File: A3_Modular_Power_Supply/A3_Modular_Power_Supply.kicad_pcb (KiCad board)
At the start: 2 copper layers, 70.9 x 86.6 mm, 81 parts, among them J1 JST-XH, J10 JST-XH, J11 JST-XH, J12 JST-XH, J13 JST-XH, J14 JST-XH, J15 JST-XH, J16 JST-XH, J17 FX30B-3S-7.62DSA, J18 FX30B-3S-7.62DSA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

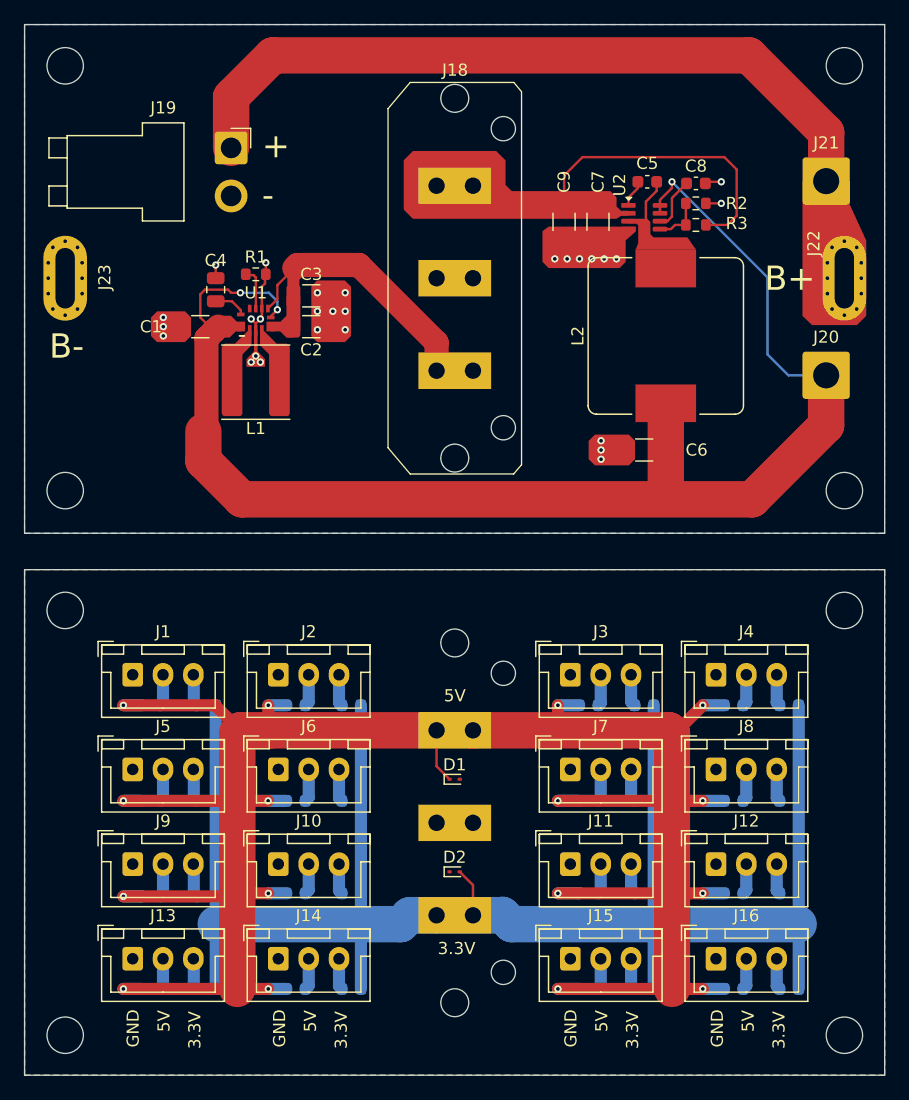
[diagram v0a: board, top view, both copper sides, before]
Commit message: Resized board to match flight computer Switched to single PCB
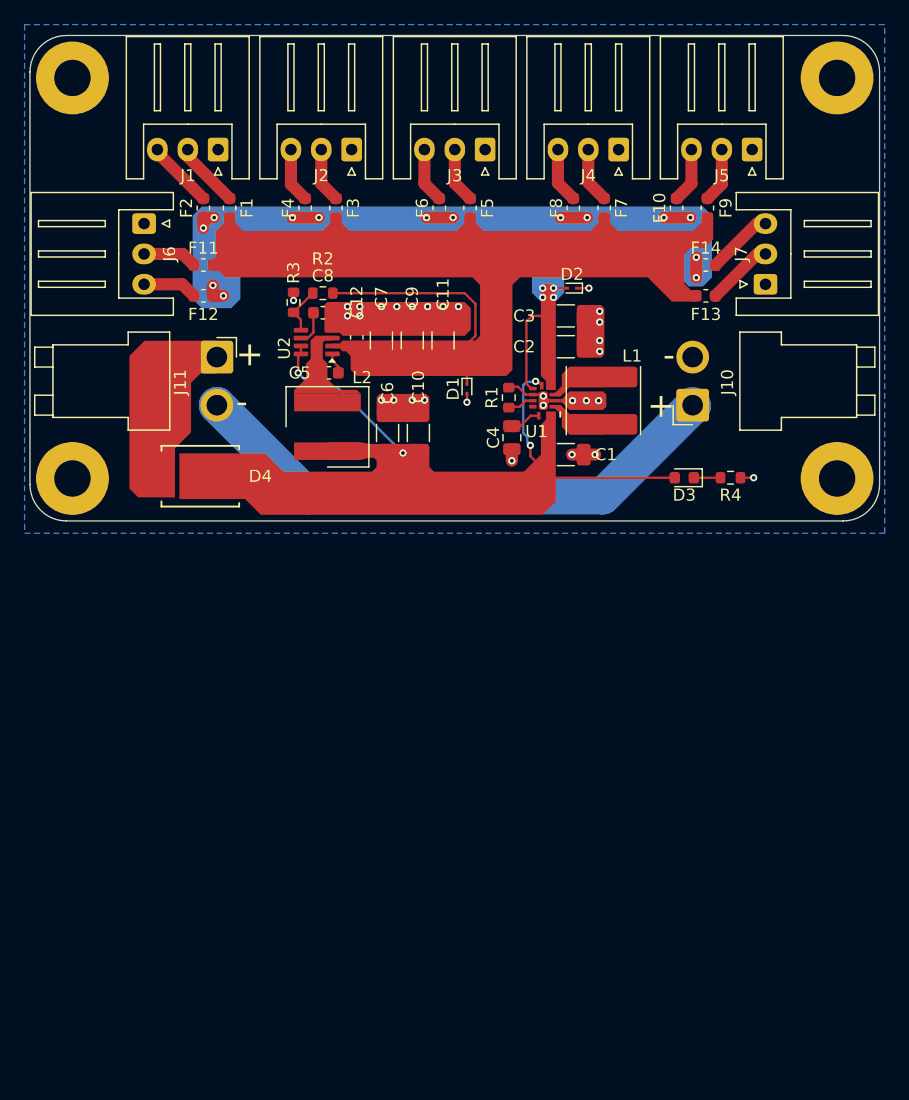
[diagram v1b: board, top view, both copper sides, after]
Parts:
- removed F15, F16, F17, F18, F19, F20, F21, F22, F23, F24, F25, F26, F27, F28, F29, F30, F31, F32: 1A, Fuse:Fuse_0603_1608Metric
- removed the J11 at (159.5, 123.3)
- removed J12, J13, J14, J15, J16, J8, J9: JST-XH, Connector_JST:JST_XH_B3B-XH-A_1x03_P2.50mm_Vertical
- removed J17, J18: FX30B-3S-7.62DSA, MPS_footprints:FX30B-3x-7.62
- removed J20: SWITCH-, Connector_Wire:SolderWire-1.5sqmm_1x01_D1.7mm_OD3.9mm
- removed J21: SWITCH+, Connector_Wire:SolderWire-1.5sqmm_1x01_D1.7mm_OD3.9mm
- removed J22: BATT+, MPS_footprints:Nickle_Strip
- removed J23: BATT-, MPS_footprints:Nickle_Strip
- removed the REF** at (182.1, 137.4)
- removed the REF** at (117.9, 102.4)
- removed the REF** at (182.1, 102.4)
- removed the REF** at (117.9, 137.4)
- removed the REF** at (117.9, 57.5)
- removed the REF** at (182.1, 57.5)
- removed the REF** at (117.9, 92.5)
- removed the REF** at (182.1, 92.5)
- added C10: 10uF, Capacitor_SMD:C_1206_3216Metric, F.Cu at (147.0, 87.8)
- added C11: 10uF, Capacitor_SMD:C_1206_3216Metric, F.Cu at (149.0, 80.1)
- added C12: 0.1uF, Capacitor_SMD:C_0603_1608Metric, F.Cu at (141.9, 79.9)
- added D3: LED, LED_SMD:LED_0603_1608Metric, F.Cu at (168.9, 91.4)
- added D4: STPS1045SFY, MPS_footprints:PSMCTO-277A_STM, F.Cu at (129.0, 91.3)
- added R4: 120R, Resistor_SMD:R_0603_1608Metric, F.Cu at (172.7, 91.4)
- added REF**: MountingHole_3mm_Pad, MountingHole:MountingHole_3mm_Pad, F.Cu at (181.5, 91.5)
- added REF**: MountingHole_3mm_Pad, MountingHole:MountingHole_3mm_Pad, F.Cu at (118.5, 91.5)
- added REF**: MountingHole_3mm_Pad, MountingHole:MountingHole_3mm_Pad, F.Cu at (181.5, 58.5)
- added REF**: MountingHole_3mm_Pad, MountingHole:MountingHole_3mm_Pad, F.Cu at (118.5, 58.5)
- F1, F10, F11, F12, F13, F14, F2, F3, F4, F5, F6, F7, F8, F9: moved to F.Cu
- J1, J2, J3, J4, J5, J6, J7: footprint Connector_JST:JST_XH_B3B-XH-A_1x03_P2.50mm_Vertical -> Connector_JST:JST_XH_S3B-XH-A_1x03_P2.50mm_Horizontal
- J10: value JST-XH -> BATT; footprint Connector_JST:JST_XH_B3B-XH-A_1x03_P2.50mm_Vertical -> Connector_JST:JST_VH_B2PS-VH_1x02_P3.96mm_Horizontal
- J11: renamed from J19; value Charge -> SWITCH
- L2: footprint Inductor_SMD:L_Bourns_SRP1245A -> MPS_footprints:L_Wurth_WE-XHMI-6060P
- moved J5 72.2 mm to (174.5, 64.4), turned to 180 degrees
- moved F9 67.0 mm to (170.8, 69.2), turned to -90 degrees
- moved F10 62.4 mm to (168.3, 69.2), turned to -90 degrees
- moved J10 50.9 mm to (169.6, 85.5), turned to 90 degrees
- moved D2 49.0 mm to (159.7, 75.8), turned to 180 degrees
- moved J6 46.3 mm to (124.4, 70.5), turned to -90 degrees
- moved F11 44.8 mm to (129.3, 73.9), turned to 0 degrees
- moved F8 44.7 mm to (159.8, 69.2), turned to -90 degrees
- moved F14 44.4 mm to (170.7, 73.9), turned to 180 degrees
- moved F6 44.3 mm to (148.7, 69.2), turned to -90 degrees
- moved J4 44.0 mm to (163.5, 64.4), turned to 180 degrees
- moved J1 43.8 mm to (130.5, 64.4), turned to 180 degrees
- moved J3 43.8 mm to (152.5, 64.4), turned to 180 degrees
- moved J2 43.7 mm to (141.5, 64.4), turned to 180 degrees
- moved F12 43.4 mm to (129.3, 76.5)
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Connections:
- C2 pad 1: Net-(J18-Pin_1) -> /3V3
- C3 pad 1: Net-(J18-Pin_1) -> /3V3
- C7 pad 1: Net-(J18-Pin_3) -> /5V
- C9 pad 1: Net-(J18-Pin_3) -> /5V
- D1 pad 2: /GND -> -BATT
- D2 pad 1: /GND -> -BATT
- J1 pad 1: /GND -> -BATT
- J10 pad 1: /GND -> Net-(J10-Pin_1)
- J10 pad 2: Net-(J10-Pin_2) -> -BATT
- J11 pad 2: -BATT -> Net-(J10-Pin_1)
- J2 pad 1: /GND -> -BATT
- J3 pad 1: /GND -> -BATT
- J4 pad 1: /GND -> -BATT
- J5 pad 1: /GND -> -BATT
- J6 pad 1: /GND -> -BATT
- J7 pad 1: /GND -> -BATT
- R2 pad 1: Net-(J18-Pin_3) -> /5V
- U1 pad 4: Net-(J18-Pin_1) -> /3V3
- U1 pad 6: Net-(J18-Pin_1) -> /3V3
- U2 pad 2: Net-(J18-Pin_3) -> /5V
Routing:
- net /5V: track 198.7 -> 22.5 mm, vias 16 -> 0
- net /3V3: track 146.2 -> 22.8 mm, vias 0 -> 18
- net +BATT: track 117.3 -> 32.6 mm, vias 3 -> 4
- net Net-(J11-Pin_1): track 61.3 -> 0.00 mm
- net Net-(J10-Pin_1): track 0.00 -> 45.5 mm
- net Net-(J18-Pin_3): track 26.6 -> 0.00 mm
- net Net-(J18-Pin_1): track 23.3 -> 0.00 mm
- net Net-(U2-SW): track 5.05 -> 0.00 mm
- net Net-(J1-Pin_3): track 2.63 -> 5.60 mm
- net Net-(J7-Pin_2): track 2.67 -> 5.56 mm
- net Net-(J1-Pin_2): track 2.60 -> 5.45 mm
- net Net-(J7-Pin_3): track 2.71 -> 5.54 mm
- net Net-(J9-Pin_3): track 2.77 -> 0.00 mm
- net Net-(J9-Pin_2): track 2.75 -> 0.00 mm
- net Net-(J8-Pin_2): track 2.70 -> 0.00 mm
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- removed copper zone on B.Cu, net /GND
- removed copper zone on F.Cu, net /GND
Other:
- board size 70.9 x 86.6 mm -> 70 x 40 mm
- board text removed: "3.3V"
- board text removed: "5V"
- board text removed: "B+"
- board text removed: "B-"
- board text removed: "GND"

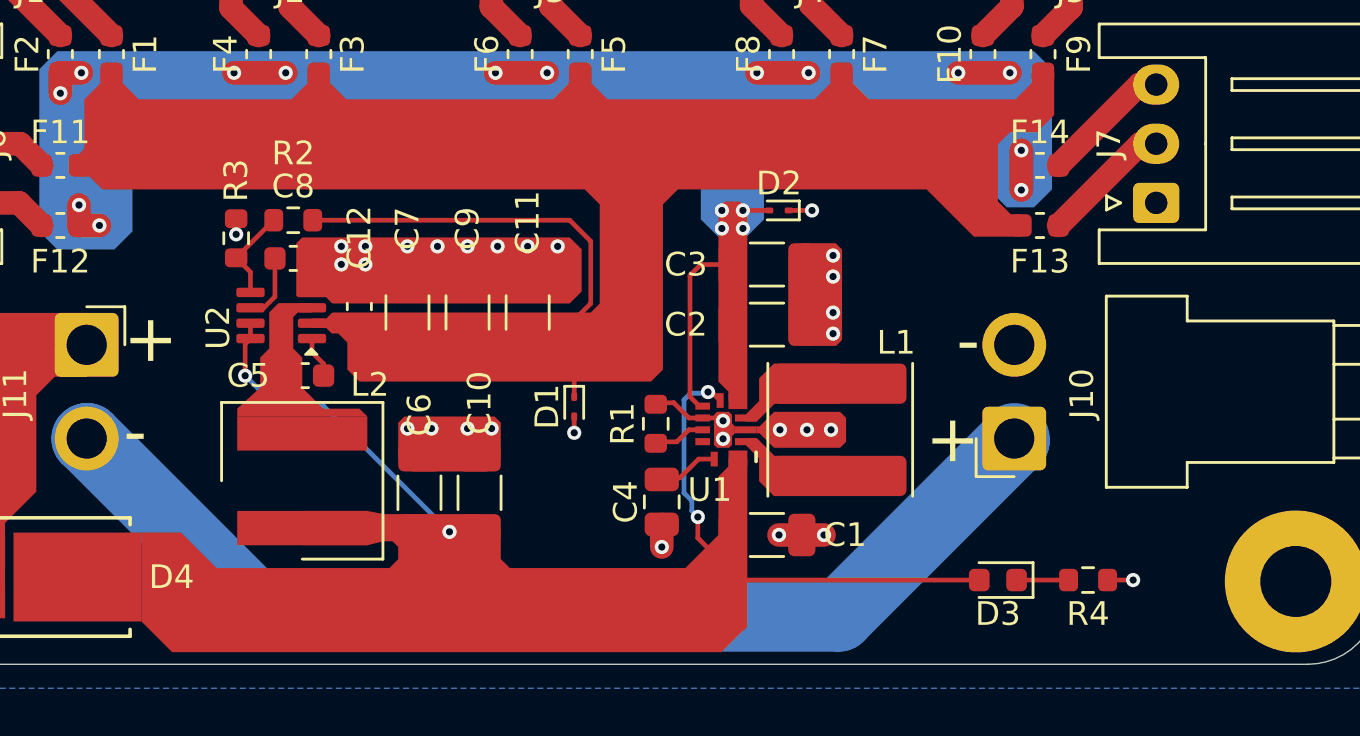
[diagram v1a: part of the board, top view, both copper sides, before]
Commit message: Added power indication LEDs
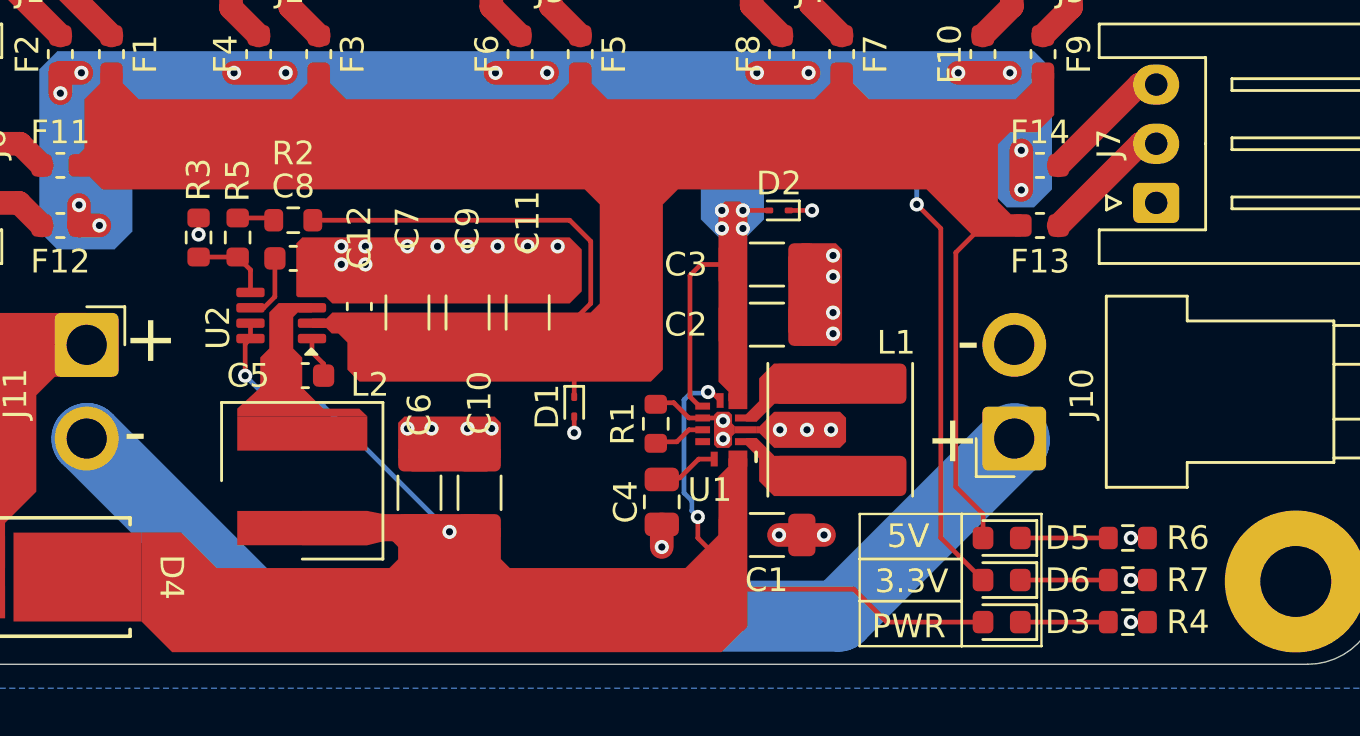
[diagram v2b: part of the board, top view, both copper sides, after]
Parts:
- added D5: LED, LED_SMD:LED_0603_1608Metric, F.Cu at (169.1, 89.7)
- added D6: LED, LED_SMD:LED_0603_1608Metric, F.Cu at (169.1, 91.4)
- added R5: 200k, Resistor_SMD:R_0603_1608Metric, F.Cu at (136.8, 77.0)
- added R6: 120R, Resistor_SMD:R_0603_1608Metric, F.Cu at (174.4, 89.7)
- added R7: 120R, Resistor_SMD:R_0603_1608Metric, F.Cu at (174.4, 91.4)
- R2: value 400k -> 200k
- moved R4 2.45 mm to (174.4, 93.2)
- moved D3 1.79 mm to (169.1, 93.2)
- moved R3 1.59 mm to (135.1, 77.0)
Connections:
- R2 pad 2: Net-(U2-FB) -> Net-(R2-Pad2)
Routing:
- net /3V3: track 22.8 -> 42.4 mm, vias 18 -> 19
- net /5V: track 22.5 -> 36.3 mm
- net Net-(D6-K): track 0.00 -> 3.72 mm
- net Net-(D5-K): track 0.00 -> 3.72 mm
- net -BATT: track 9.42 -> 11.2 mm, vias 30 -> 32
- net Net-(R2-Pad2): track 0.00 -> 1.56 mm
- net Net-(D3-K): track 2.20 -> 3.72 mm
- net +BATT: track 32.6 -> 33.2 mm
- net Net-(U2-FB): track 3.96 -> 3.37 mm
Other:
- board text added: "3.3V"
- board text added: "5V"
- board text added: "PWR"
